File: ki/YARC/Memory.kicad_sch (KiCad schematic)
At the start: 15 parts, among them U100 74LS32, U14 74LS20, U18 AS6C6264, U20 74HC00, U21 74LS08, U22 74LS139, U23 74LS32, U24 AS6C6264, U25 74HC245, U26 74LS157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

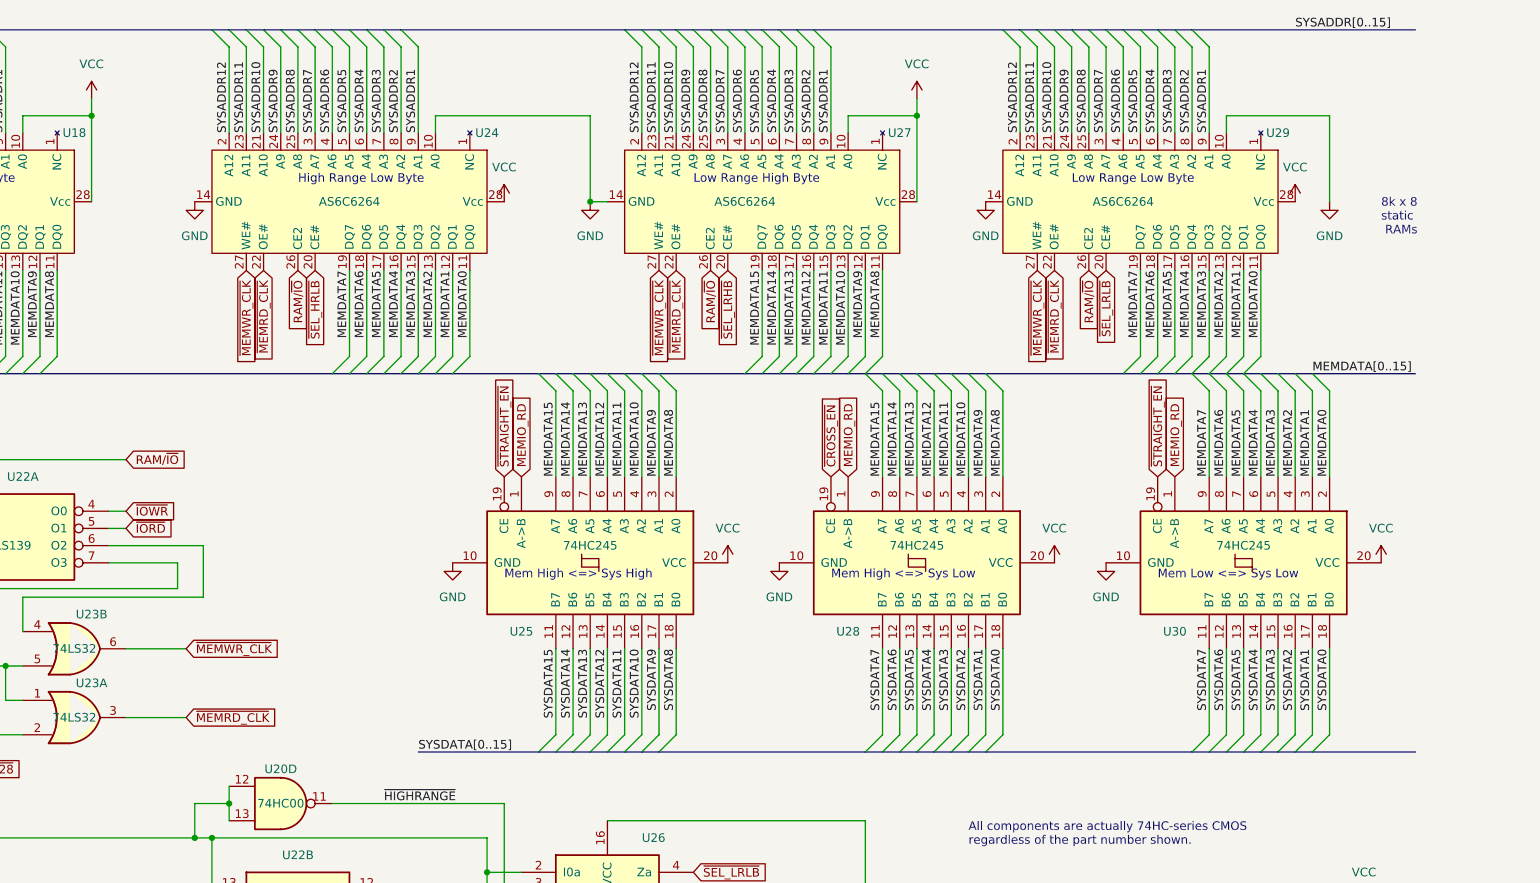
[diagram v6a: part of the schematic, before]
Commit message: Removed about 2/3 of 2300+ errors from the ERC
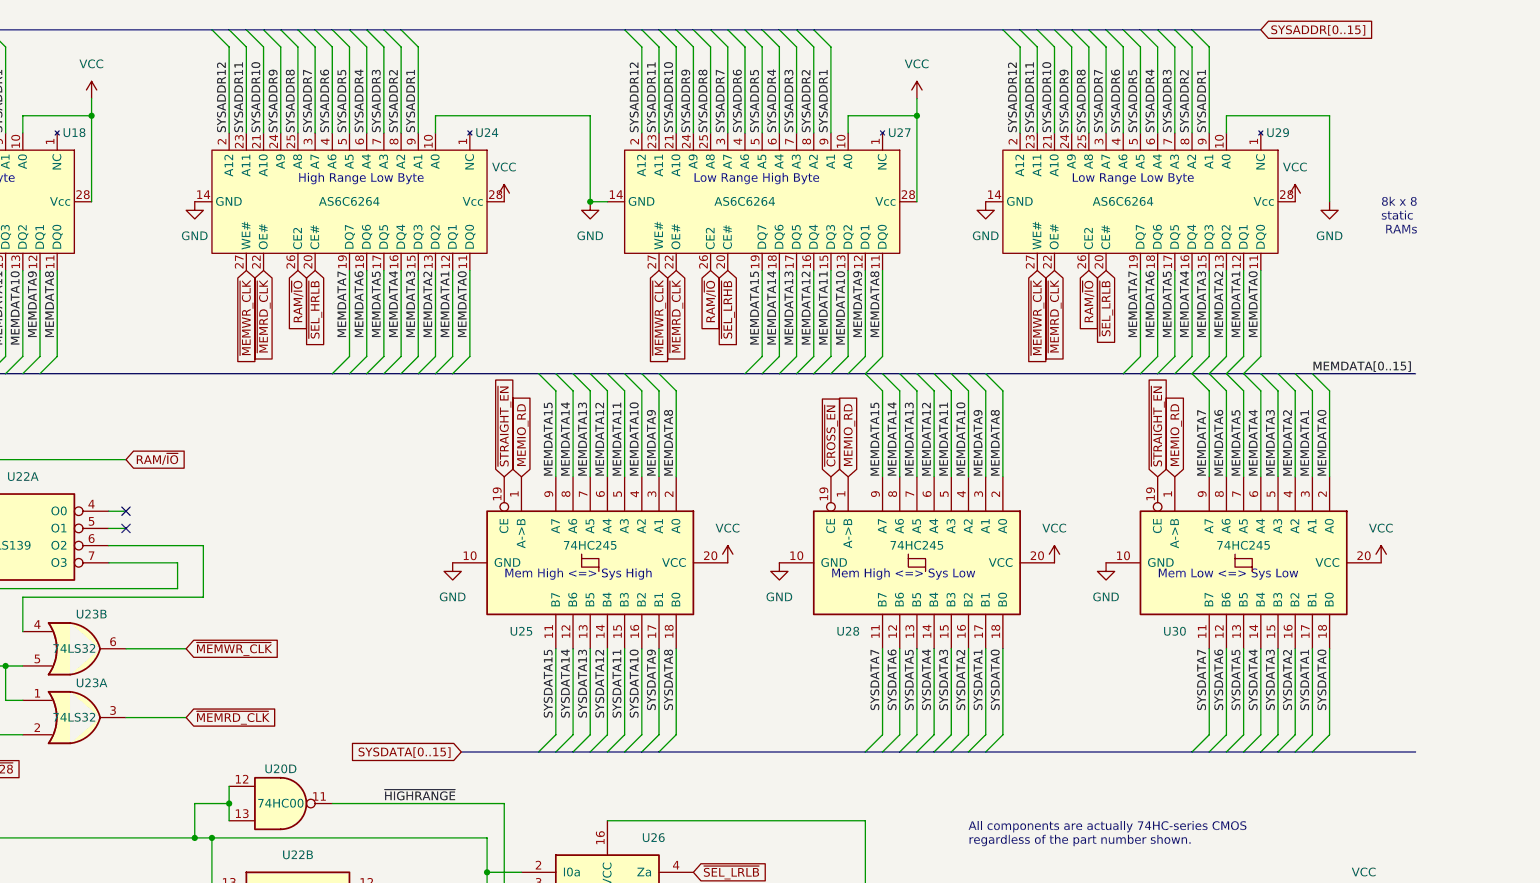
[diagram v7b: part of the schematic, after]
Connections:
- net ~{IORD}: no longer names the net of U22.5 (O1)
- net ~{IOWR}: no longer names the net of U22.4 (O0)
- no-connect marks 0 -> 2
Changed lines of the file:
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@@
   (junction (at 200.66 144.78) (diameter 0) (color 0 0 0 0)
   )
+  (no_connect (at 73.66 86.36))
+  (no_connect (at 73.66 88.9))
   (bus_entry (at 152.4 15.24) (size 2.54 2.54)
     (stroke (width 0) (type default))
@@
     (stroke (width 0) (type default))
   )
-  (bus (pts (xy 116.84 121.92) (xy 134.62 121.92))
+  (bus (pts (xy 123.19 121.92) (xy 134.62 121.92))
     (stroke (width 0) (type default))
   )
@@
     (stroke (width 0) (type default))
   )
-  (bus (pts (xy 231.14 15.24) (xy 264.16 15.24))
+  (bus (pts (xy 231.14 15.24) (xy 241.3 15.24))
     (stroke (width 0) (type default))
   )
@@
     (effects (font (size 1.27 1.27)) (justify right bottom))
   )
-  (label "SYSADDR[0..15]" (at 246.38 15.24 0) (fields_autoplaced)
-    (effects (font (size 1.27 1.27)) (justify left bottom))
-  )
   (label "MEMDATA15" (at 137.16 81.28 90) (fields_autoplaced)
     (effects (font (size 1.27 1.27)) (justify left bottom))
@@
   )
   (label "MEMDATA12" (at 193.04 81.28 90) (fields_autoplaced)
-    (effects (font (size 1.27 1.27)) (justify left bottom))
-  )
-  (label "SYSDATA[0..15]" (at 116.84 121.92 0) (fields_autoplaced)
     (effects (font (size 1.27 1.27)) (justify left bottom))
   )
@@
     )
   )
+  (global_label "SYSDATA[0..15]" (shape input) (at 123.19 121.92 180) (fields_autoplaced)
+    (effects (font (size 1.27 1.27)) (justify right))
+    (property "Intersheetrefs" "${INTERSHEET_REFS}" (at 105.7509 121.92 0)
+      (effects (font (size 1.27 1.27)) (justify right) hide)
+    )
+  )
   (global_label "MEMIO_RD" (shape input) (at 132.08 81.28 90) (fields_autoplaced)
     (effects (font (size 1.27 1.27)) (justify left))
@@
     )
   )
-  (global_label "~{IOWR}" (shape input) (at 73.66 86.36 0) (fields_autoplaced)
-    (effects (font (size 1.27 1.27)) (justify left))
-    (property "Intersheetrefs" "${INTERSHEET_REFS}" (at 80.7298 86.2806 0)
-      (effects (font (size 1.27 1.27)) (justify left) hide)
-    )
-  )
   (global_label "~{MEMWR_CLK}" (shape input) (at 30.48 50.8 270) (fields_autoplaced)
     (effects (font (size 1.27 1.27)) (justify right))
@@
     )
   )
-  (global_label "~{IORD}" (shape input) (at 73.66 88.9 0) (fields_autoplaced)
-    (effects (font (size 1.27 1.27)) (justify left))
-    (property "Intersheetrefs" "${INTERSHEET_REFS}" (at 80.5483 88.8206 0)
-      (effects (font (size 1.27 1.27)) (justify left) hide)
-    )
-  )
   (global_label "~{MEMIO_EN}" (shape input) (at 30.48 99.06 180) (fields_autoplaced)
     (effects (font (size 1.27 1.27)) (justify right))
@@
       (effects (font (size 1.27 1.27)) (justify left) hide)
     )
+  )
+  (global_label "SYSADDR[0..15]" (shape input) (at 241.3 15.24 0) (fields_autoplaced)
+    (effects (font (size 1.27 1.27)) (justify left))
+    (property "Intersheetrefs" "${INTERSHEET_REFS}" (at 259.2229 15.24 0)
+      (effects (font (size 1.27 1.27)) (justify left) hide)
+    )

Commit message: Continuing cleanup of schematic
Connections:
- net SYSCLK6 renamed SYSCLK
- no-connect marks 2 -> 4
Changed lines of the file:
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@@
   (junction (at 200.66 144.78) (diameter 0) (color 0 0 0 0)
   )
+  (no_connect (at 198.12 180.34))
   (no_connect (at 73.66 86.36))
+  (no_connect (at 177.8 180.34))
   (no_connect (at 73.66 88.9))
   (bus_entry (at 152.4 15.24) (size 2.54 2.54)
@@
     )
   )
-  (global_label "SYSCLK6" (shape input) (at 90.17 166.37 180) (fields_autoplaced)
+  (global_label "SYSCLK" (shape input) (at 90.17 166.37 180) (fields_autoplaced)
     (effects (font (size 1.27 1.27)) (justify right))
-    (property "Intersheetrefs" "${INTERSHEET_REFS}" (at 79.4717 166.2906 0)
+    (property "Intersheetrefs" "${INTERSHEET_REFS}" (at 80.1091 166.37 0)
       (effects (font (size 1.27 1.27)) (justify right) hide)
     )
@@
     )
   )
-  (global_label "SYSCLK6" (shape input) (at 27.94 109.22 180) (fields_autoplaced)
+  (global_label "SYSCLK" (shape input) (at 27.94 109.22 180) (fields_autoplaced)
     (effects (font (size 1.27 1.27)) (justify right))
-    (property "Intersheetrefs" "${INTERSHEET_REFS}" (at 17.2417 109.1406 0)
+    (property "Intersheetrefs" "${INTERSHEET_REFS}" (at 17.8791 109.22 0)
       (effects (font (size 1.27 1.27)) (justify right) hide)
     )
